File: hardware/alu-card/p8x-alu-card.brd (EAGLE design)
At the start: 160 x 100 mm, 77 parts, among them J1 FABC96R, U1 A REG, U10 ALU HI, U11 CLA, U12 SH1 LO, U13 SH1 HI, U14 SH2 LO, U15 SH2 HI, U16 ALU OUT, U17 FLAGS, U18 Z DET, U19 74HCT08, U2 A OUT, U20 DOE DEC, U21 DLD DEC, U22 FLAG MUX, U23 FLAG OUT, U24 74HCT32, U25 74HCT00, U26 C FLAG FF, U27 BUS Z-DET, U28 SHIFT-OUT MUX, U29 C-SRC MUX, U3 B REG, U30 SHIN MUX, U31 74HCT08 CLK/FORCE, U32 B-MUX LO, U33 B-MUX HI, U34 74HCT86 V-XOR, U35 74HCT08 V-AND, U4 B OUT, U5 T REG, U6 T OUT, U7 T2 REG, U8 T2 OUT, U9 ALU LO

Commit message: feat(hw): card DIN connector mounting holes (DIN96C, standard DIN 41612)
The card edge connector (FABC96R) needs board mounting holes; the footprint had
only the 96 signal pins. Split the connector into two packages so cards and the
backplane don't share holes:
- DIN96C (card): 96 pins + 2 mounting holes on the centreline (x=2.54), 94.0mm
  apart, drill 2.8mm for M2.5. Emitted as non-plated <hole> elements (new
  lib_xml branch for MH* entries). DEV["DIN96C"] = DIN96 pins, pkg DIN96C.
- DIN96 (backplane receptacle): pins only, unchanged.
Card J1 (all 6: 5 plug-in via card() + memory) now uses DIN96C; backplane slots
keep DIN96. Fixed card() to honor the J1 package on the board side and in CARDS
(was hardcoding "DIN96", which both dropped the holes and mislabeled the BOM).

Verified: each card .brd has 2 holes, backplane 0; overlap guard clean (the
shared-package version collided with backplane terminators); BOM shows 6 card
(DIN96C) + 10 backplane. All boards 0 errors, all 6 suites pass.

VERIFY the 94mm spacing / 2.8mm dia against the FABC96R datasheet.

Co-Authored-By: Claude Opus 4.8 <noreply@anthropic.com>
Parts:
- J1: device p8x:DIN96 -> p8x:DIN96C
- moved U33 130.5 mm to (17.9, -13.0)
- moved RP1 12.9 mm to (66.5, -13.0)
- moved CD33 12.9 mm to (29.8, -13.1)
- moved CD34 12.9 mm to (46.0, -13.1)
- moved CD35 12.9 mm to (62.2, -13.1)
- moved LED3 12.9 mm to (81.0, -13.1)
- moved LED4 12.9 mm to (102.3, -13.1)
- moved R4 12.9 mm to (87.8, -13.0)
- moved R5 12.9 mm to (109.1, -13.0)
- moved U34 12.9 mm to (34.1, -13.0)
- moved U35 12.9 mm to (50.3, -13.0)
- moved LED5 12.9 mm to (123.6, -13.1)
- moved J1 8.20 mm to (5.40, 87.0)
- moved CD15 1.10 mm to (142.4, 68.0)
- moved CD23 1.10 mm to (131.5, 35.9)
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
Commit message: fix(hardware): connect IC power pins on the card()-built boards
Schematic-review fix. card() wired the edge-connector and decoupling-cap pins to
VCC/GND but never added each IC's own VCC/GND supply pin, so on control, regbank,
ALU, I/O, and CF the chips' power pads were not members of the power pours and
would not have been powered. (The hand-built memory card already did this; the
backplane has no ICs. validate() couldn't catch it — it checks pin-name legality,
not connectivity.)

- card(): append (ref,"VCC")/(ref,"GND") for every IC, skipping any pin already
  wired by hand (idempotent — avoids duplicate pinrefs, e.g. ALU U16 GND)
- regenerated all 7 boards (.sch/.brd), 0 validation errors
- board-level audit: every IC on every card now has both VCC and GND on the
  power signals
- BACKLOG: moved the critical item to DONE; theory docs' power-pin callouts
  updated to "fixed"

Co-Authored-By: Claude Opus 4.8 <noreply@anthropic.com>
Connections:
- net GND: now also U1.10, U10.12, U11.8, U12.8, U13.8, U14.8, U15.8, U16.10, U17.8, U18.7, U19.7, U2.10, U20.8, U21.8, U22.8, U23.10, U24.7, U25.7, U26.7, U27.7, U28.8, U29.8, U3.10, U30.8, U31.7, U32.8, U33.8, U34.7, U35.7, U4.10, U5.10, U6.10, U7.10, U8.10, U9.12
- net VCC: now also U1.20, U10.24, U11.16, U12.16, U13.16, U14.16, U15.16, U16.20, U17.16, U18.14, U19.14, U2.20, U20.16, U21.16, U22.16, U23.20, U24.14, U25.14, U26.14, U27.14, U28.16, U29.16, U3.20, U30.16, U31.14, U32.16, U33.16, U34.14, U35.14, U4.20, U5.20, U6.20, U7.20, U8.20, U9.24
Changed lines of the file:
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@@
 <contactref element="CD34" pad="2"/>
 <contactref element="CD35" pad="2"/>
+<contactref element="U1" pad="10"/>
+<contactref element="U2" pad="10"/>
+<contactref element="U3" pad="10"/>
+<contactref element="U4" pad="10"/>
+<contactref element="U5" pad="10"/>
+<contactref element="U6" pad="10"/>
+<contactref element="U7" pad="10"/>
+<contactref element="U8" pad="10"/>
+<contactref element="U9" pad="12"/>
+<contactref element="U10" pad="12"/>
+<contactref element="U11" pad="8"/>
+<contactref element="U12" pad="8"/>
+<contactref element="U13" pad="8"/>
+<contactref element="U14" pad="8"/>
+<contactref element="U15" pad="8"/>
+<contactref element="U16" pad="10"/>
+<contactref element="U17" pad="8"/>
+<contactref element="U18" pad="7"/>
+<contactref element="U19" pad="7"/>
+<contactref element="U20" pad="8"/>
+<contactref element="U21" pad="8"/>
+<contactref element="U22" pad="8"/>
+<contactref element="U23" pad="10"/>
+<contactref element="U24" pad="7"/>
+<contactref element="U25" pad="7"/>
+<contactref element="U26" pad="7"/>
+<contactref element="U27" pad="7"/>
+<contactref element="U28" pad="8"/>
+<contactref element="U29" pad="8"/>
+<contactref element="U30" pad="8"/>
+<contactref element="U31" pad="7"/>
+<contactref element="U32" pad="8"/>
+<contactref element="U33" pad="8"/>
+<contactref element="U34" pad="7"/>
+<contactref element="U35" pad="7"/>
 <polygon width="0.254" layer="2" isolate="0.3" rank="1">
 <vertex x="0" y="0"/>
@@
 <contactref element="CD34" pad="1"/>
 <contactref element="CD35" pad="1"/>
+<contactref element="U1" pad="20"/>
+<contactref element="U2" pad="20"/>
+<contactref element="U3" pad="20"/>
+<contactref element="U4" pad="20"/>
+<contactref element="U5" pad="20"/>
+<contactref element="U6" pad="20"/>
+<contactref element="U7" pad="20"/>
+<contactref element="U8" pad="20"/>
+<contactref element="U9" pad="24"/>
+<contactref element="U10" pad="24"/>
+<contactref element="U11" pad="16"/>
+<contactref element="U12" pad="16"/>
+<contactref element="U13" pad="16"/>
+<contactref element="U14" pad="16"/>
+<contactref element="U15" pad="16"/>
+<contactref element="U16" pad="20"/>
+<contactref element="U17" pad="16"/>
+<contactref element="U18" pad="14"/>
+<contactref element="U19" pad="14"/>
+<contactref element="U20" pad="16"/>
+<contactref element="U21" pad="16"/>
+<contactref element="U22" pad="16"/>
+<contactref element="U23" pad="20"/>
+<contactref element="U24" pad="14"/>
+<contactref element="U25" pad="14"/>
+<contactref element="U26" pad="14"/>
+<contactref element="U27" pad="14"/>
+<contactref element="U28" pad="16"/>
+<contactref element="U29" pad="16"/>
+<contactref element="U30" pad="16"/>
+<contactref element="U31" pad="14"/>
+<contactref element="U32" pad="16"/>
+<contactref element="U33" pad="16"/>
+<contactref element="U34" pad="14"/>
+<contactref element="U35" pad="14"/>
 <polygon width="0.254" layer="15" isolate="0.3" rank="1">
 <vertex x="0" y="0"/>

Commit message: feat(backplane): row-B even pins become spare bus lines (SPARE12-23)
Row B was a solid ground guard (B3-26 all GND). Per request, B3-26 now ALTERNATE:
odd pins stay GND (still a guard between most signal pairs), and the 12 even pins
(B4,B6,..,B26) become spare bus lines SPARE12-SPARE23, routed slot-to-slot — so
new signals can be added later without re-spinning the backplane. B27-30
(CLRC/BSEL/IRQ/SPARE11) unchanged.

- busnet() updated in all three copies (gen_eagle, gen_bus_pdf, gen_bus_card)
- backplane .brd routes the 12 new spares (mirrors the B27-30 routing); odd-pin
  grounds remain on the GND pour
- every card regenerated: their connectors no longer tie the even B pins to GND
  (those are spare lines now) — they simply don't connect the spares
- all 8 boards validate (0 errors); schematic + bus PDFs regenerated
- docs updated: bus-definition (pin map + notes), backplane theory + design notes
- net signal-integrity trade noted: a solid guard shields slightly better; the
  alternation was chosen deliberately for expansion room

Co-Authored-By: Claude Opus 4.8 <noreply@anthropic.com>
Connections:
- net GND: no longer J1.B10, J1.B12, J1.B14, J1.B16, J1.B18, J1.B20, J1.B22, J1.B24, J1.B26, J1.B4, J1.B6, J1.B8
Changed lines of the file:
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@@
 <contactref element="J1" pad="A32"/>
 <contactref element="J1" pad="B3"/>
-<contactref element="J1" pad="B4"/>
 <contactref element="J1" pad="B5"/>
-<contactref element="J1" pad="B6"/>
 <contactref element="J1" pad="B7"/>
-<contactref element="J1" pad="B8"/>
 <contactref element="J1" pad="B9"/>
-<contactref element="J1" pad="B10"/>
 <contactref element="J1" pad="B11"/>
-<contactref element="J1" pad="B12"/>
 <contactref element="J1" pad="B13"/>
-<contactref element="J1" pad="B14"/>
 <contactref element="J1" pad="B15"/>
-<contactref element="J1" pad="B16"/>
 <contactref element="J1" pad="B17"/>
-<contactref element="J1" pad="B18"/>
 <contactref element="J1" pad="B19"/>
-<contactref element="J1" pad="B20"/>
 <contactref element="J1" pad="B21"/>
-<contactref element="J1" pad="B22"/>
 <contactref element="J1" pad="B23"/>
-<contactref element="J1" pad="B24"/>
 <contactref element="J1" pad="B25"/>
-<contactref element="J1" pad="B26"/>
 <contactref element="J1" pad="B31"/>
 <contactref element="J1" pad="B32"/>

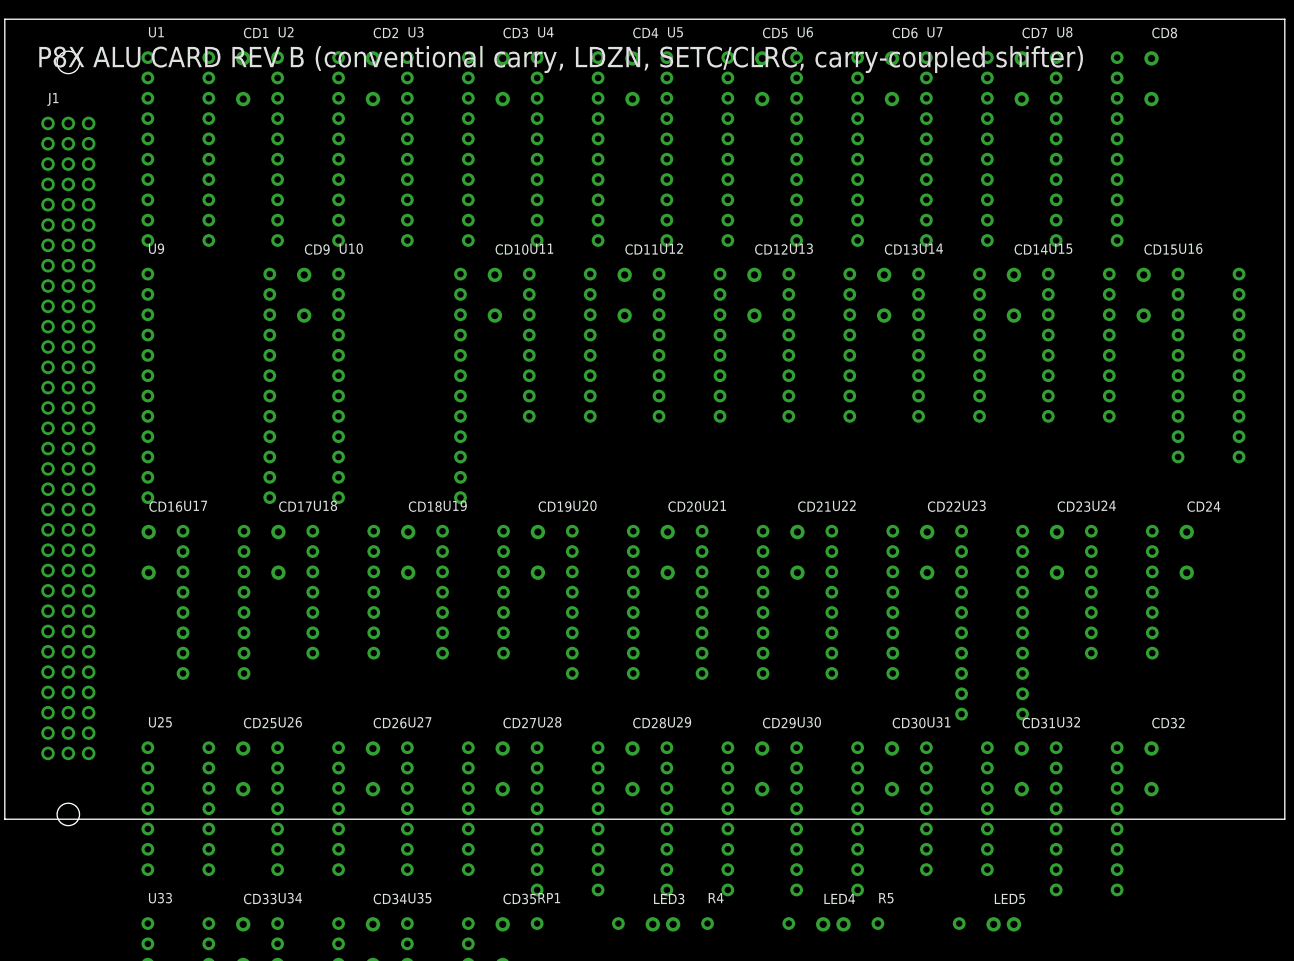
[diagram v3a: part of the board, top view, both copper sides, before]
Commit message: feat(generators): faithful Eagle/Fusion output (values, layers, smashed parts)
Make the generated .sch/.brd match how Eagle itself writes files, so Fusion
displays everything correctly (was mis-mapping names/values to scratch layers):

- devicesets get uservalue="yes" so the `value` field is honored at all (it was
  silently ignored before — no card's value ever displayed)
- emit the COMPLETE standard Eagle layer table (62 layers) in every drawing, so
  Fusion has nothing to remap on import
- board elements are now smashed="yes" with explicit NAME (tNames/25) and VALUE
  (tValues/27) attributes — refdes + part number show reliably
- add std <attributes>/<variantdefs> board sections + board-package >VALUE silk
- schematic: `value` holds the orderable part number (>VALUE + BOM); the logical
  function is placed as text near each chip via a new card() `labels` arg
- write_brd gains outline_only and unplaced modes (parts off-board + ratsnest);
  card() exposes brd_outline_only / brd_unplaced

Proven on the LED card (part numbers + function labels + an unplaced 4-layer
board). The other cards get the structural fixes now; rolling the part-number/
labels convention across them is the next step. All 8 boards validate (0 errors).

Co-Authored-By: Claude Opus 4.8 <noreply@anthropic.com>
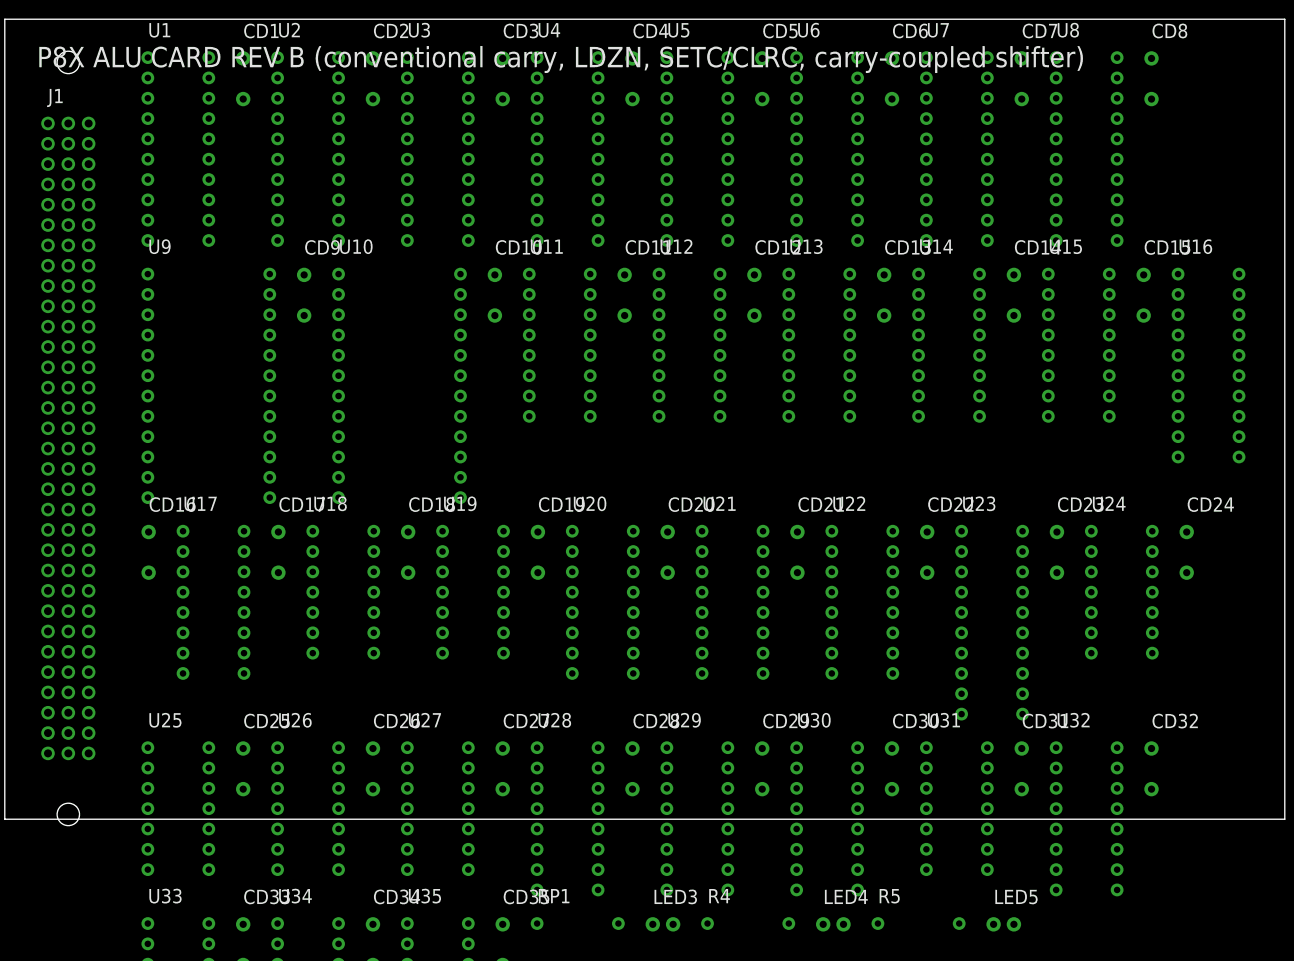
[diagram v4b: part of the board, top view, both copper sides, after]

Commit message: feat(generators): roll out part-number values + function labels to all cards
Apply the value=part-number / function-as-label convention across every card
(was proven on the LED card). A device->part-number map (PN) + a small resolver
in card() do it automatically:

- logic/memory ICs -> generic type numbers (74HCT138, 74HCT244, 28C64, 6850,
  MAX232, ...); the old per-part function text becomes the placed schematic label
- LEDs -> value = colour (GRN/YEL/RED), function -> label (POWER, RUN, HALT, ...)
- switches -> SPST, function -> label (RUN/HALT, STEP, RESET)
- headers -> 1x3 / 1x4, function -> label (CLKSEL, RTC 3-WIRE, SERIAL)
- gate arrays / passives / connectors keep their value (74HCT08, 1K, 100N,
  FABC96R, 28C256, 62256, IDE-40); a few contaminated values hand-cleaned
  (gate-array suffixes, IDE label) with explicit labels where meaningful

Net result: the Eagle `value` field is a clean orderable part number everywhere
(BOM + >VALUE + board silk), and the logical function is placed text near each
chip. Regenerated all boards + schematic PDFs; all 8 validate (0 errors).

Co-Authored-By: Claude Opus 4.8 <noreply@anthropic.com>
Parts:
- LED3: value PWR-GRN -> GRN
- LED4: value ALU-GRN -> GRN
- LED5: value LDF-YEL -> YEL
- U1: value A REG -> 74HCT377
- U10: value ALU HI -> 74HCT181
- U11: value CLA -> 74HCT182
- U12: value SH1 LO -> 74HCT157
- U13: value SH1 HI -> 74HCT157
- U14: value SH2 LO -> 74HCT157
- U15: value SH2 HI -> 74HCT157
- U16: value ALU OUT -> 74HCT244
- U18: value Z DET -> 74HCT260
- U2: value A OUT -> 74HCT244
- U20: value DOE DEC -> 74HCT138
- U21: value DLD DEC -> 74HCT138
- U22: value FLAG MUX -> 74HCT157
- U23: value FLAG OUT -> 74HCT244
- U26: value C FLAG FF -> 74HCT74
- U27: value BUS Z-DET -> 74HCT260
- U28: value SHIFT-OUT MUX -> 74HCT157
- U29: value C-SRC MUX -> 74HCT157
- U3: value B REG -> 74HCT377
- U30: value SHIN MUX -> 74HCT157
- U31: value 74HCT08 CLK/FORCE -> 74HCT08
- U32: value B-MUX LO -> 74HCT157
- U33: value B-MUX HI -> 74HCT157
- U34: value 74HCT86 V-XOR -> 74HCT86
- U35: value 74HCT08 V-AND -> 74HCT08
- U4: value B OUT -> 74HCT244
- U5: value T REG -> 74HCT377
- U6: value T OUT -> 74HCT244
- U7: value T2 REG -> 74HCT377
- U8: value T2 OUT -> 74HCT244
- U9: value ALU LO -> 74HCT181

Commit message: feat(generators): unplaced boards by default for all plug-in cards
card() now defaults brd_unplaced=True, so every plug-in card's .brd ships as
board outline + parts parked off-board + ratsnest (no auto-placement, no copper)
— placement and routing are done in Fusion, so the generated layout was throwaway
anyway. The backplane is hand-built (not via card()) and keeps its placed,
routed layout. All 8 boards validate (0 errors).

Co-Authored-By: Claude Opus 4.8 <noreply@anthropic.com>
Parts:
- moved CD12 185.4 mm to (279.1, 68.0)
- moved CD14 185.4 mm to (311.5, 68.0)
- moved CD21 185.4 mm to (284.5, 35.9)
- moved CD28 185.4 mm to (263.9, 8.84)
- moved CD4 185.4 mm to (263.9, 95.1)
- moved R5 185.4 mm to (294.5, -13.0)
- moved U24 185.4 mm to (321.2, 36.0)
- moved U29 185.4 mm to (268.2, 8.94)
- moved U31 185.4 mm to (300.6, 8.94)
- moved U5 185.4 mm to (268.2, 95.2)
- moved U7 185.4 mm to (300.6, 95.2)
- moved CD10 185.4 mm to (246.7, 68.0)
- moved CD16 185.4 mm to (203.4, 35.9)
- moved CD23 185.4 mm to (316.9, 35.9)
- moved CD30 185.4 mm to (296.3, 8.84)
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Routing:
- removed copper zone on layer 2, net GND
- removed copper zone on layer 15, net VCC
